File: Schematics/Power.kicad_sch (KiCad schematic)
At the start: 10 parts, among them U2 LDL1117-3.3

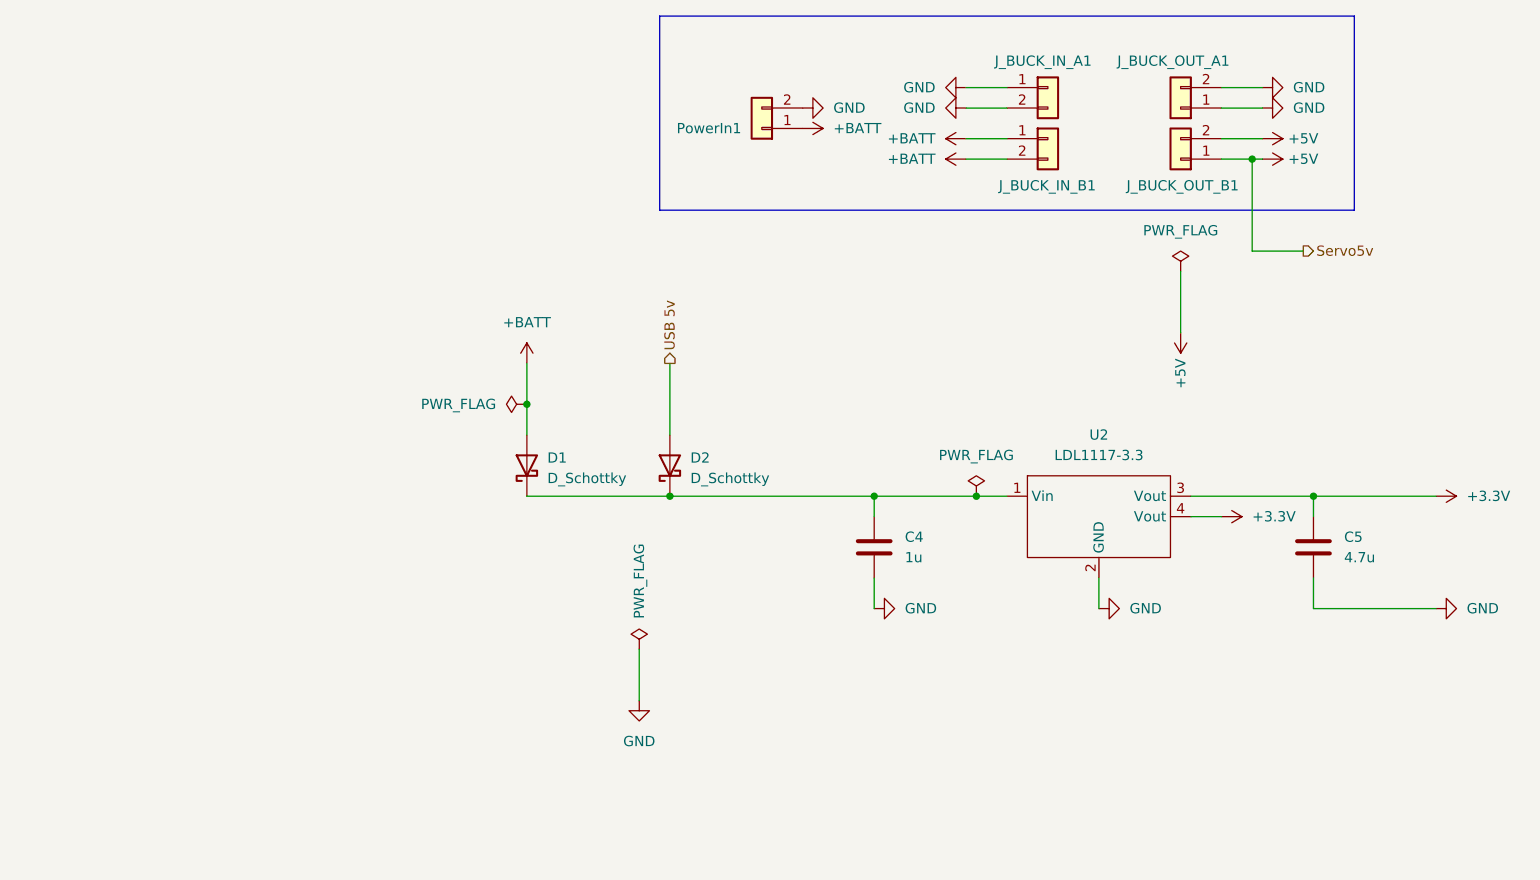
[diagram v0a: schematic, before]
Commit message: started new design with esp32
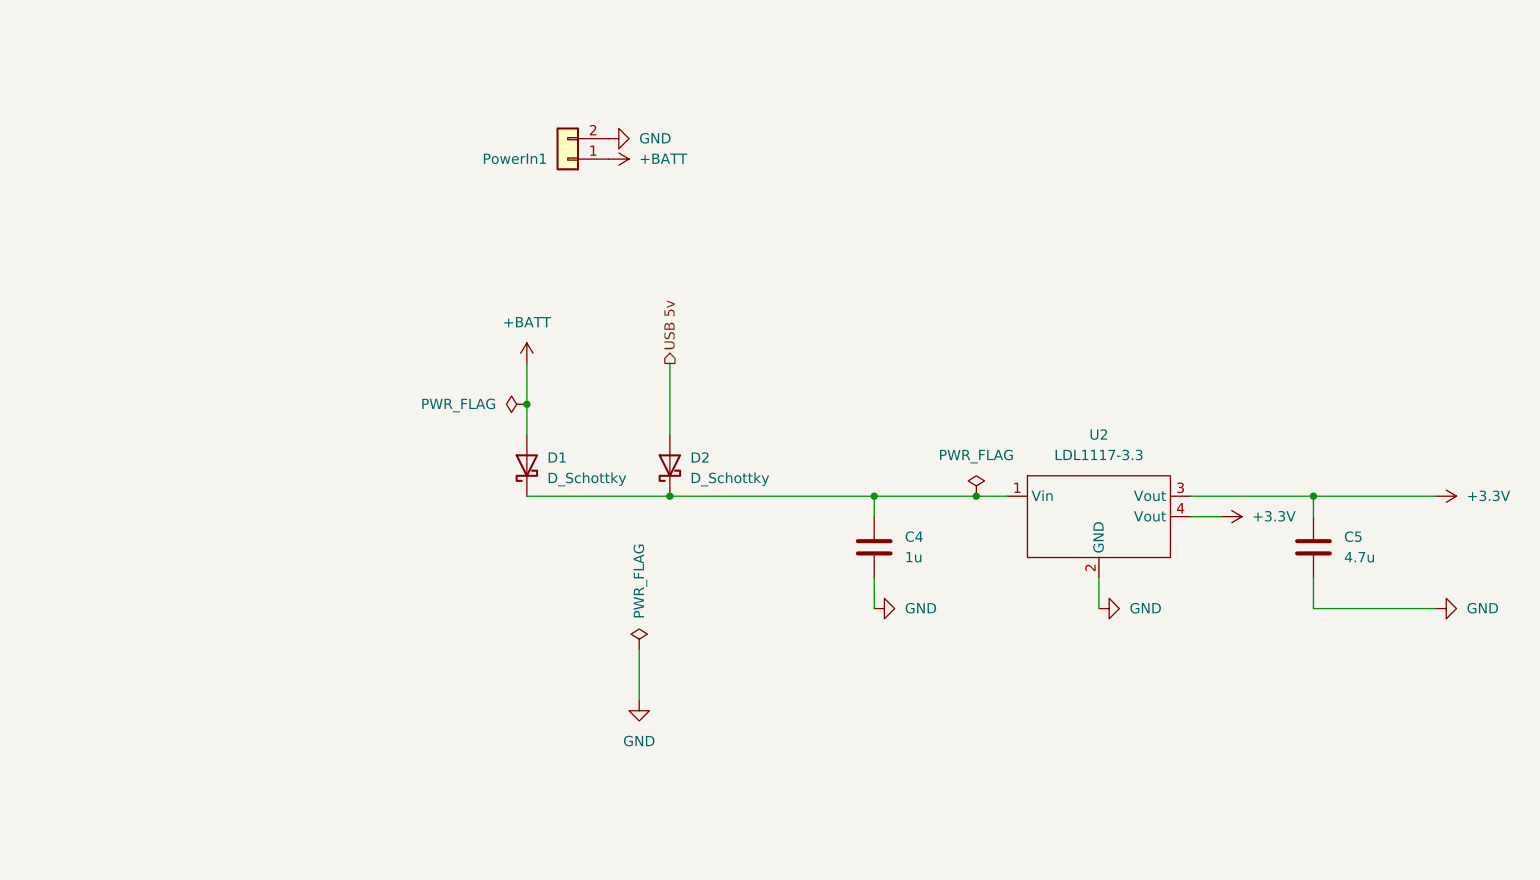
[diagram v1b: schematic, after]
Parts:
- removed J_BUCK_IN_A1, J_BUCK_IN_B1, J_BUCK_OUT_A1, J_BUCK_OUT_B1: ~, Connector_PinSocket_2.54mm:PinSocket_1x02_P2.54mm_Horizontal, symbol Connector_Generic:Conn_01x02
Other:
- moved on the sheet: PowerIn1

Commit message: final draft, in JLPCB cart
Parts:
- PowerIn1: now left out of the parts list
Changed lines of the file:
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@@
+			)
+		)
+		(property "SnapEDA_Link" ""
+			(at 156.21 133.35 0)
+			(hide yes)
+			(show_name no)
+			(do_not_autoplace no)
+			(effects
+				(font
+					(size 1.27 1.27)
+				)
+			)
+		)
+		(property "DESCRIPTION" ""
+			(at 156.21 133.35 0)
+			(hide yes)
+			(show_name no)
+			(do_not_autoplace no)
+			(effects
+				(font
+					(size 1.27 1.27)
+				)
 			)
 		)
@@
 			)
 		)
-		(property "Description" "Unpolarized capacitor"
+		(property "Description" ""
 			(at 127 119.38 0)
 			(hide yes)
@@
 		)
 		(property "LCSC" "C28323"
+			(at 127 119.38 0)
+			(hide yes)
+			(show_name no)
+			(do_not_autoplace no)
+			(effects
+				(font
+					(size 1.27 1.27)
+				)
+			)
+		)
+		(property "SnapEDA_Link" ""
+			(at 127 119.38 0)
+			(hide yes)
+			(show_name no)
+			(do_not_autoplace no)
+			(effects
+				(font
+					(size 1.27 1.27)
+				)
+			)
+		)
+		(property "DESCRIPTION" ""
 			(at 127 119.38 0)
 			(hide yes)
@@
 			)
 		)
-		(property "Description" "Unpolarized capacitor"
+		(property "Description" ""
 			(at 181.61 119.38 0)
 			(hide yes)
@@
 		)
 		(property "LCSC" "C98192"
+			(at 181.61 119.38 0)
+			(hide yes)
+			(show_name no)
+			(do_not_autoplace no)
+			(effects
+				(font
+					(size 1.27 1.27)
+				)
+			)
+		)
+		(property "SnapEDA_Link" ""
+			(at 181.61 119.38 0)
+			(hide yes)
+			(show_name no)
+			(do_not_autoplace no)
+			(effects
+				(font
+					(size 1.27 1.27)
+				)
+			)
+		)
+		(property "DESCRIPTION" ""
 			(at 181.61 119.38 0)
 			(hide yes)
@@
 			)
 		)
-		(property "Description" "Schottky diode"
-			(at 83.82 109.22 0)
+		(property "Description" ""
+			(at 83.82 109.22 90)
 			(hide yes)
 			(show_name no)
@@
 		)
 		(property "MP" ""
+			(at 83.82 109.22 90)
+			(hide yes)
+			(show_name no)
+			(do_not_autoplace no)
+			(effects
+				(font
+					(size 1.27 1.27)
+				)
+			)
+		)
+		(property "SnapEDA_Link" ""
+			(at 83.82 109.22 90)
+			(hide yes)
+			(show_name no)
+			(do_not_autoplace no)
+			(effects
+				(font
+					(size 1.27 1.27)
+				)
+			)
+		)
+		(property "DESCRIPTION" ""
 			(at 83.82 109.22 90)
 			(hide yes)
@@
 		(body_style 1)
 		(exclude_from_sim no)
-		(in_bom yes)
+		(in_bom no)
 		(on_board yes)
 		(in_pos_files yes)
@@
 			)
 		)
-		(property "Description" "Generic connector, single row, 01x02, script generated (kicad-library-utils/schlib/autogen/connector/)"
+		(property "Description" ""
 			(at 88.9 71.12 0)
 			(hide yes)
@@
 		)
 		(property "LCSC" "C17644051"
+			(at 88.9 71.12 0)
+			(hide yes)
+			(show_name no)
+			(do_not_autoplace no)
+			(effects
+				(font
+					(size 1.27 1.27)
+				)
+			)
+		)
+		(property "SnapEDA_Link" ""
+			(at 88.9 71.12 0)
+			(hide yes)
+			(show_name no)
+			(do_not_autoplace no)
+			(effects
+				(font
+					(size 1.27 1.27)
+				)
+			)
+		)
+		(property "DESCRIPTION" ""
 			(at 88.9 71.12 0)
 			(hide yes)
@@
 			)
 		)
-		(property "Description" "Schottky diode"
-			(at 101.6 109.22 0)
+		(property "Description" ""
+			(at 101.6 109.22 90)
 			(hide yes)
 			(show_name no)
@@
 			(at 101.6 109.22 90)
 			(hide yes)
+			(show_name no)
+			(do_not_autoplace no)
+			(effects
+				(font
+					(size 1.27 1.27)
+				)
+			)
+		)
+		(property "SnapEDA_Link" ""
+			(at 101.6 109.22 90)
+			(hide yes)
+			(show_name no)
+			(do_not_autoplace no)
+			(effects
+				(font
+					(size 1.27 1.27)
+				)
+			)
+		)
+		(property "DESCRIPTION" ""
+			(at 101.6 109.22 90)
+			(hide yes)

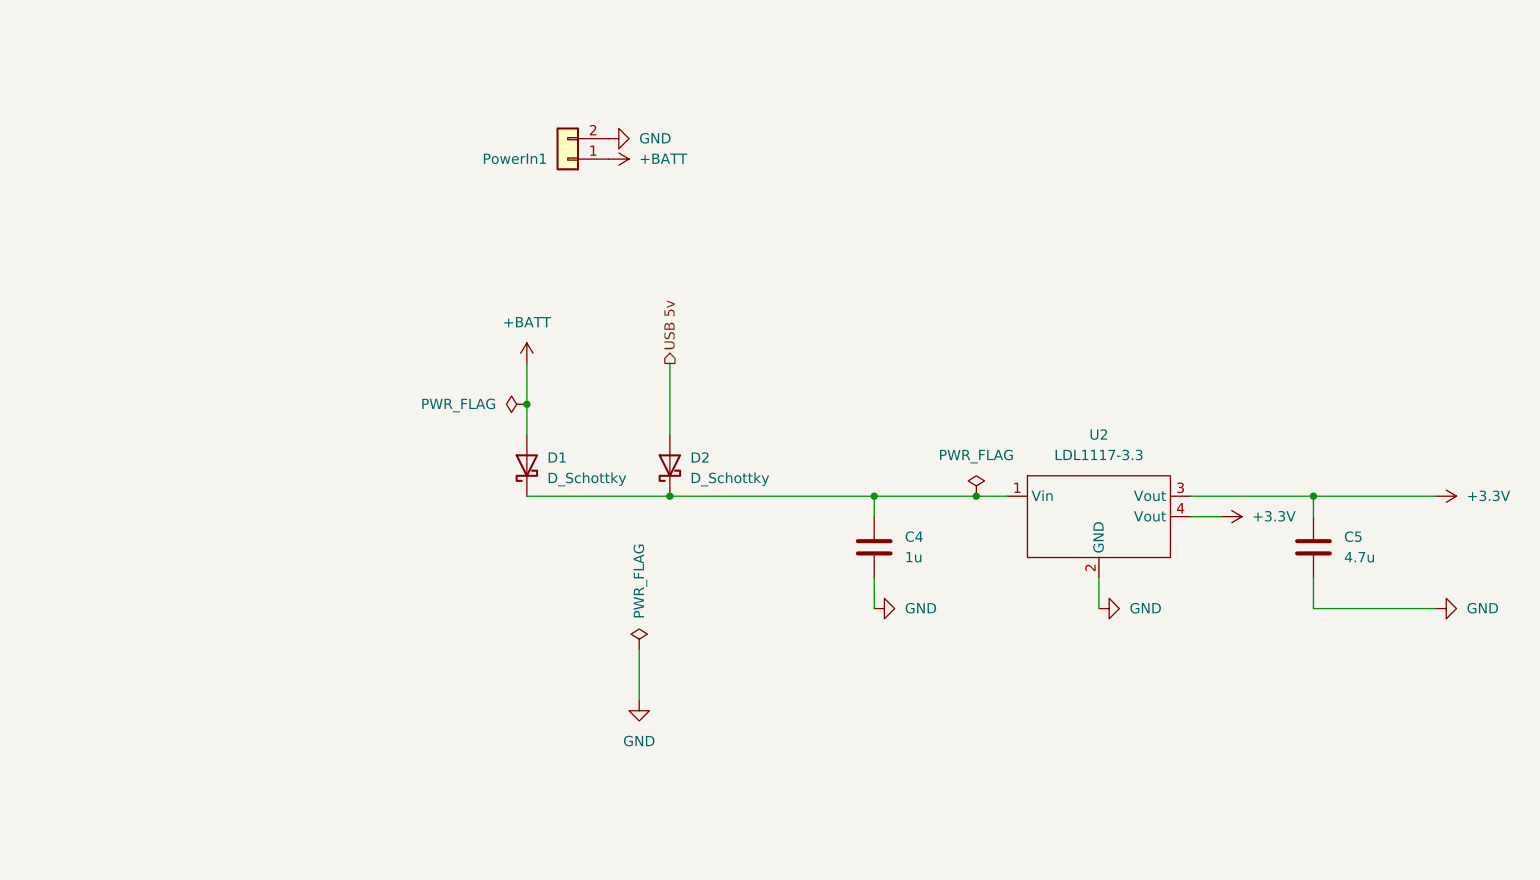
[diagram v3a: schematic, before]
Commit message: Added encoder connection for parafoil motor position information, in buy order ready for purchase
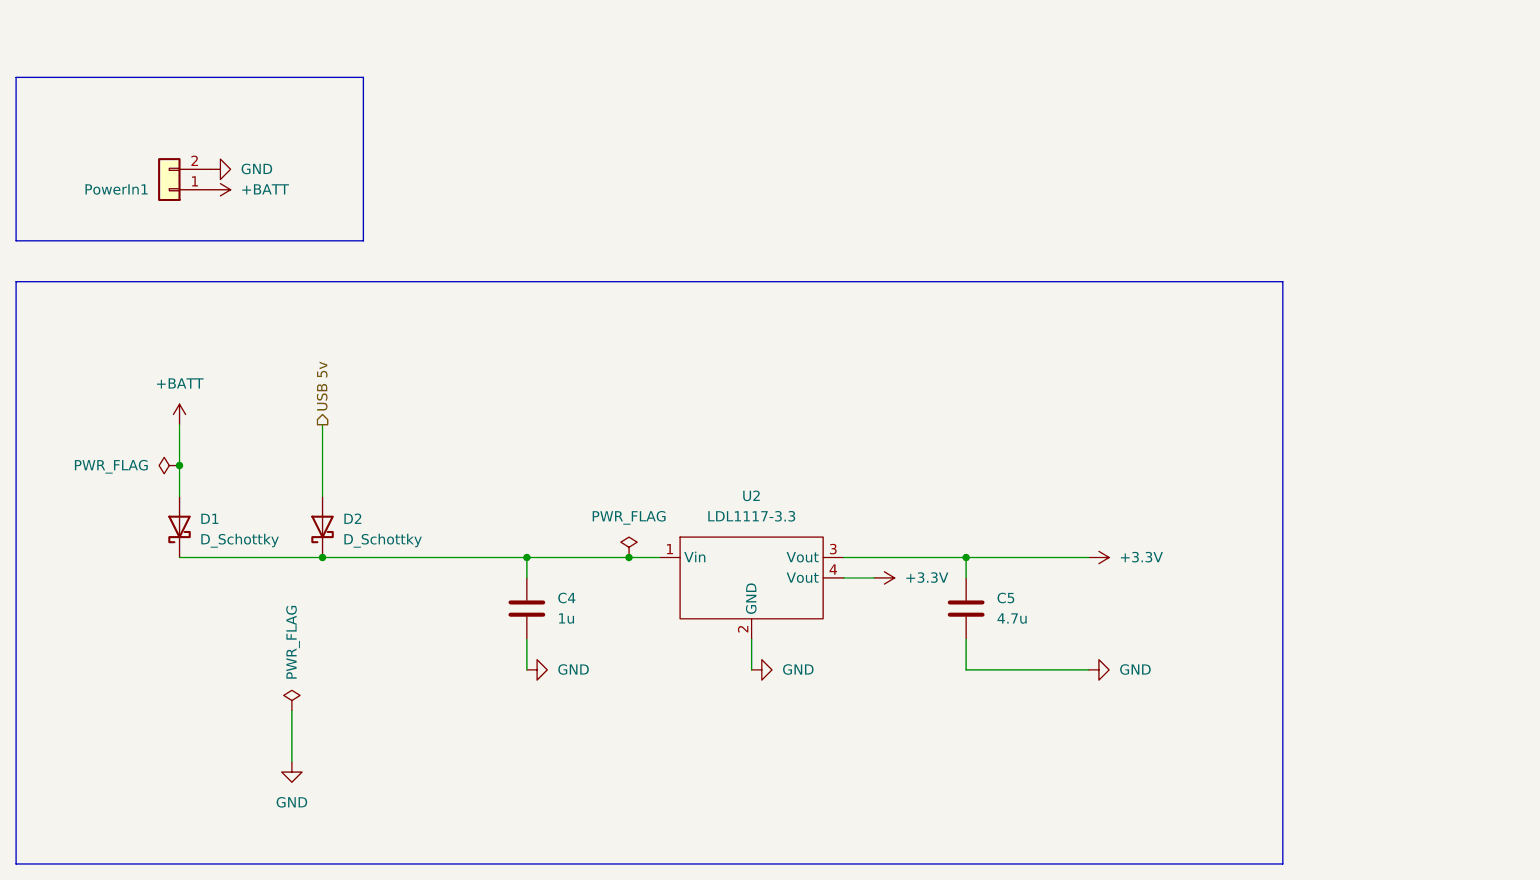
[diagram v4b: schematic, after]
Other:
- moved on the sheet: C4, C5, D1, D2, PowerIn1, U2
